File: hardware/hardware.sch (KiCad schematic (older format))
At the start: 55 parts, among them J1 BATT, J2 RFID-RC522, J3 104031-0811, J4 PROG, J5 Conn_01x06_Male, J6 PCM5102A_1, J7 PCM5102A_2, J8 Speakers, SW1 Vol down, SW2 Vol up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

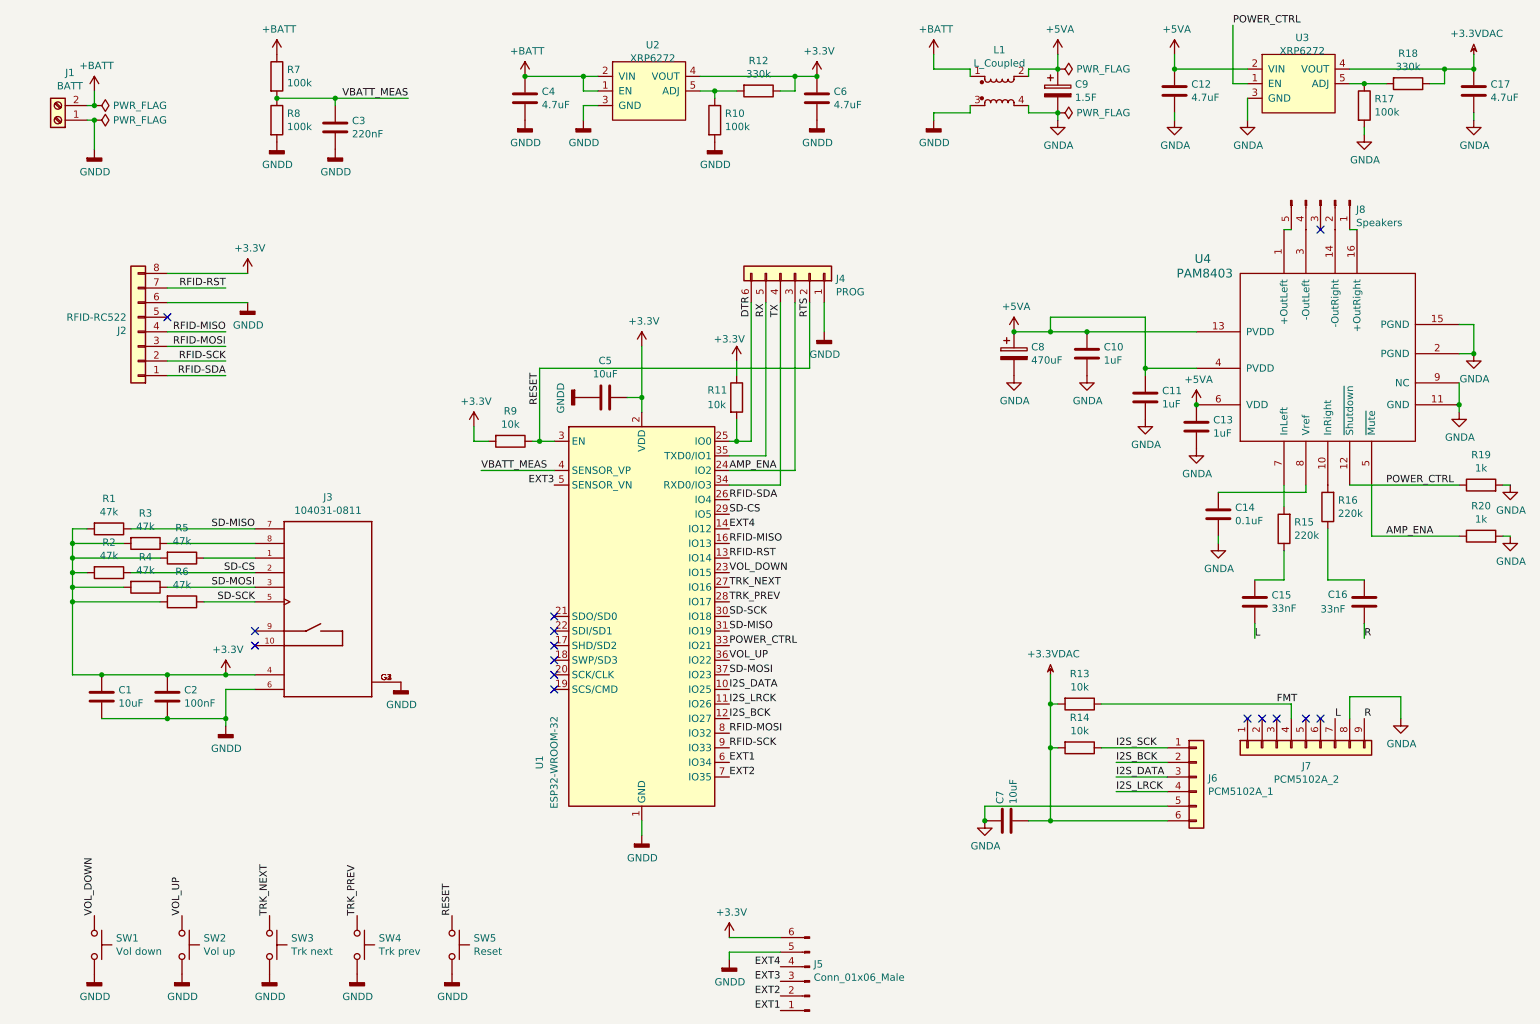
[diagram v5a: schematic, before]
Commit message: assign footprints, generate netlist
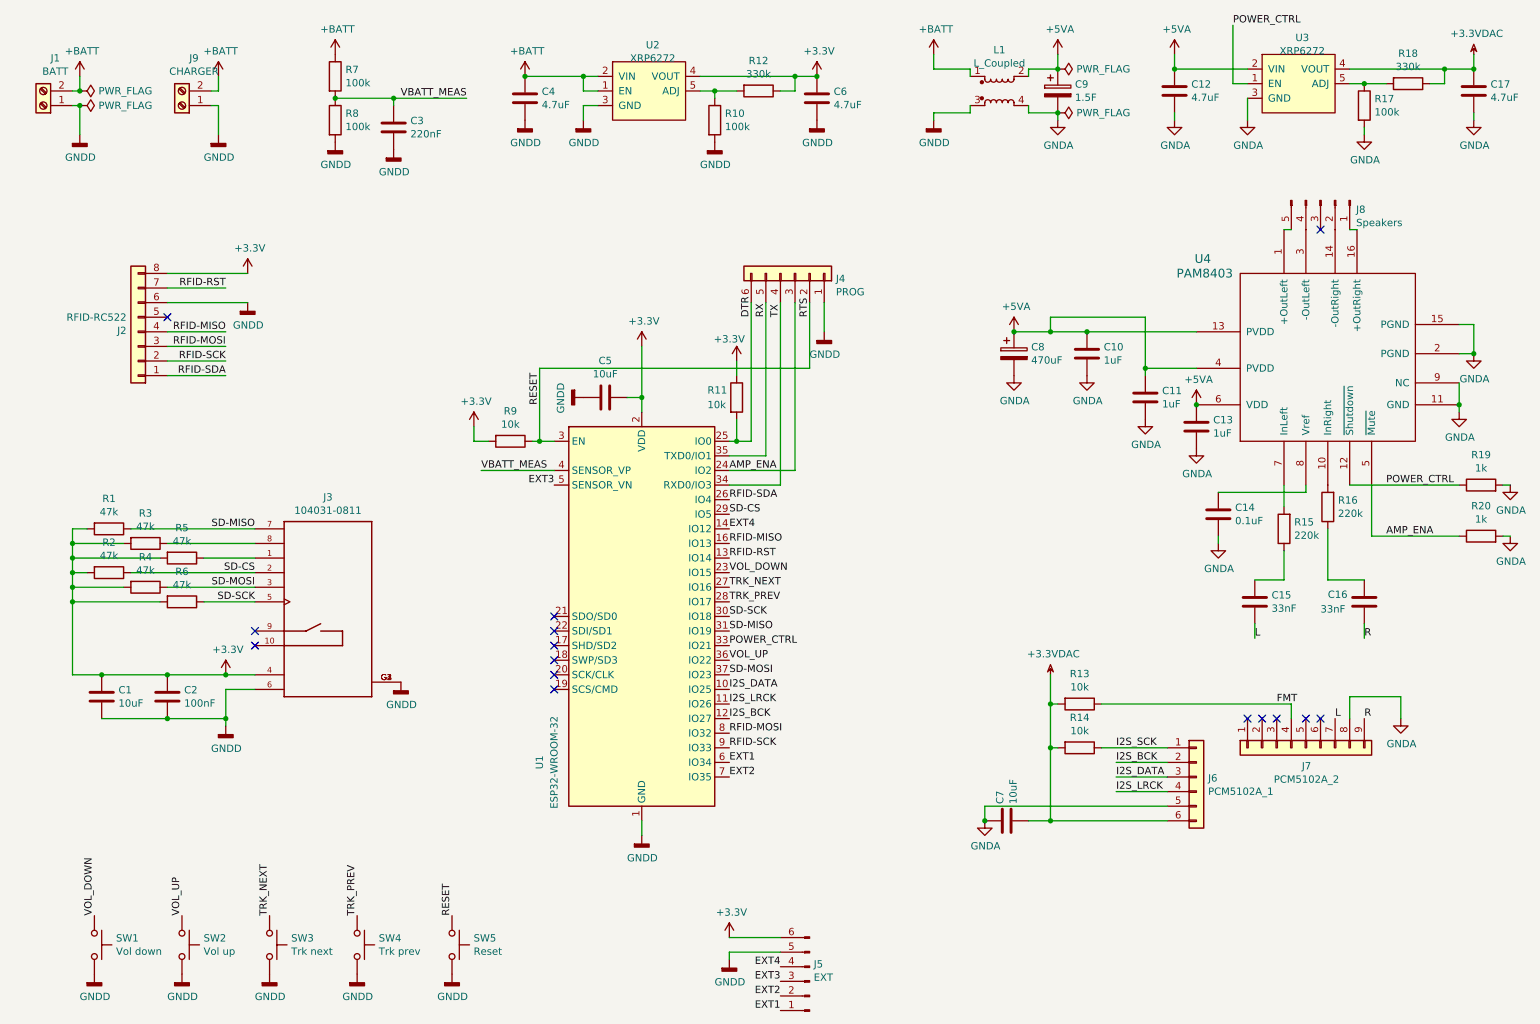
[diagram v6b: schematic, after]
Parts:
- added J9: CHARGER, Connector_PinHeader_2.54mm:PinHeader_1x02_P2.54mm_Vertical, symbol Connector:Screw_Terminal_01x02
- C1, C5, C7: footprint (none) -> Capacitor_SMD:C_0805_2012Metric_Pad1.15x1.40mm_HandSolder
- C10, C11, C13: footprint (none) -> Capacitor_THT:C_Rect_L4.6mm_W5.5mm_P2.50mm_MKS02_FKP02
- C12, C17, C4, C6: footprint (none) -> Capacitor_SMD:C_1206_3216Metric_Pad1.42x1.75mm_HandSolder
- C14, C15, C16, C2, C3: footprint (none) -> Capacitor_THT:C_Disc_D3.0mm_W1.6mm_P2.50mm
- C8: footprint (none) -> Capacitor_THT:CP_Radial_D8.0mm_P3.80mm
- C9: footprint (none) -> Capacitor_THT:C_Rect_L16.5mm_W4.7mm_P15.00mm_MKT
- J1: footprint (none) -> Connector_PinHeader_2.54mm:PinHeader_1x02_P2.54mm_Vertical
- J2: footprint (none) -> Connector_PinSocket_2.54mm:PinSocket_1x08_P2.54mm_Vertical
- J4: footprint (none) -> Connector_PinSocket_2.54mm:PinSocket_1x06_P2.54mm_Horizontal
- J5: value Conn_01x06_Male -> EXT; footprint (none) -> Connector_PinHeader_2.54mm:PinHeader_2x03_P2.54mm_Vertical
- J6: footprint (none) -> Connector_PinSocket_2.54mm:PinSocket_1x06_P2.54mm_Vertical
- J7: footprint (none) -> Connector_PinSocket_2.54mm:PinSocket_1x09_P2.54mm_Vertical
- J8: footprint (none) -> Connector_PinHeader_2.54mm:PinHeader_1x05_P2.54mm_Horizontal
- L1: footprint (none) -> Inductor_THT:Choke_Schaffner_RN212-04-12.5x18.0mm
- R1, R10, R11, R12, R13, R14, R15, R16, R17, R18, R19, R2, R20, R3, R4, R5, R6, R7, R8, R9: footprint (none) -> Resistor_SMD:R_0612_1632Metric_Pad1.18x3.40mm_HandSolder
- SW1, SW2, SW3, SW4, SW5: footprint (none) -> Button_Switch_SMD:SW_Push_1P1T_NO_6x6mm_H9.5mm
- U2, U3: footprint (none) -> Package_TO_SOT_SMD:TO-252-5_TabPin3
- U4: footprint (none) -> Package_SO:SOP-16_4.55x10.3mm_P1.27mm
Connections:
- net +BATT: now also J9.2 (Pin_2)
- net GNDD: now also J9.1 (Pin_1)
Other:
- moved on the sheet: C3, J1, R7, R8

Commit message: fix footprint for choke
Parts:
- L1: footprint Inductor_THT:Choke_Schaffner_RN212-04-12.5x18.0mm -> choke:Choke_21x17mm
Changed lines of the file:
@@
 F 0 "L1" H 7350 1431 50  0000 C CNN
 F 1 "L_Coupled" H 7350 1340 50  0000 C CNN
-F 2 "Inductor_THT:Choke_Schaffner_RN212-04-12.5x18.0mm" H 7350 1150 50  0001 C CNN
+F 2 "choke:Choke_21x17mm" H 7350 1150 50  0001 C CNN
 F 3 "~" H 7350 1150 50  0001 C CNN
 	1    7350 1150

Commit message: [wip] board layout
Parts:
- J2: footprint Connector_PinSocket_2.54mm:PinSocket_1x08_P2.54mm_Vertical -> RFID-RC522:RFID-RC522-Module
- J3: footprint MOLEX_104031-0811 -> SDSlot:1040310811
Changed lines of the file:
@@
 F 0 "J2" H 1530 2792 50  0000 L CNN
 F 1 "RFID-RC522" H 1530 2701 50  0000 L CNN
-F 2 "Connector_PinSocket_2.54mm:PinSocket_1x08_P2.54mm_Vertical" H 1450 2800 50  0001 C CNN
+F 2 "RFID-RC522:RFID-RC522-Module" H 1450 2800 50  0001 C CNN
 F 3 "~" H 1450 2800 50  0001 C CNN
 	1    1450 2800
@@
 F 0 "J3" H 2750 5467 50  0000 C CNN
 F 1 "104031-0811" H 2750 5376 50  0000 C CNN
-F 2 "MOLEX_104031-0811" H 2750 4700 50  0001 L BNN
+F 2 "SDSlot:1040310811" H 2750 4700 50  0001 L BNN
 F 3 "1.17 USD" H 2750 4700 50  0001 L BNN
 F 4 "104031-0811" H 2750 4700 50  0001 L BNN "MP"
